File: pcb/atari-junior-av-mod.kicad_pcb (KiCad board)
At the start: 2 copper layers, 50 x 17.5 mm, 36 parts

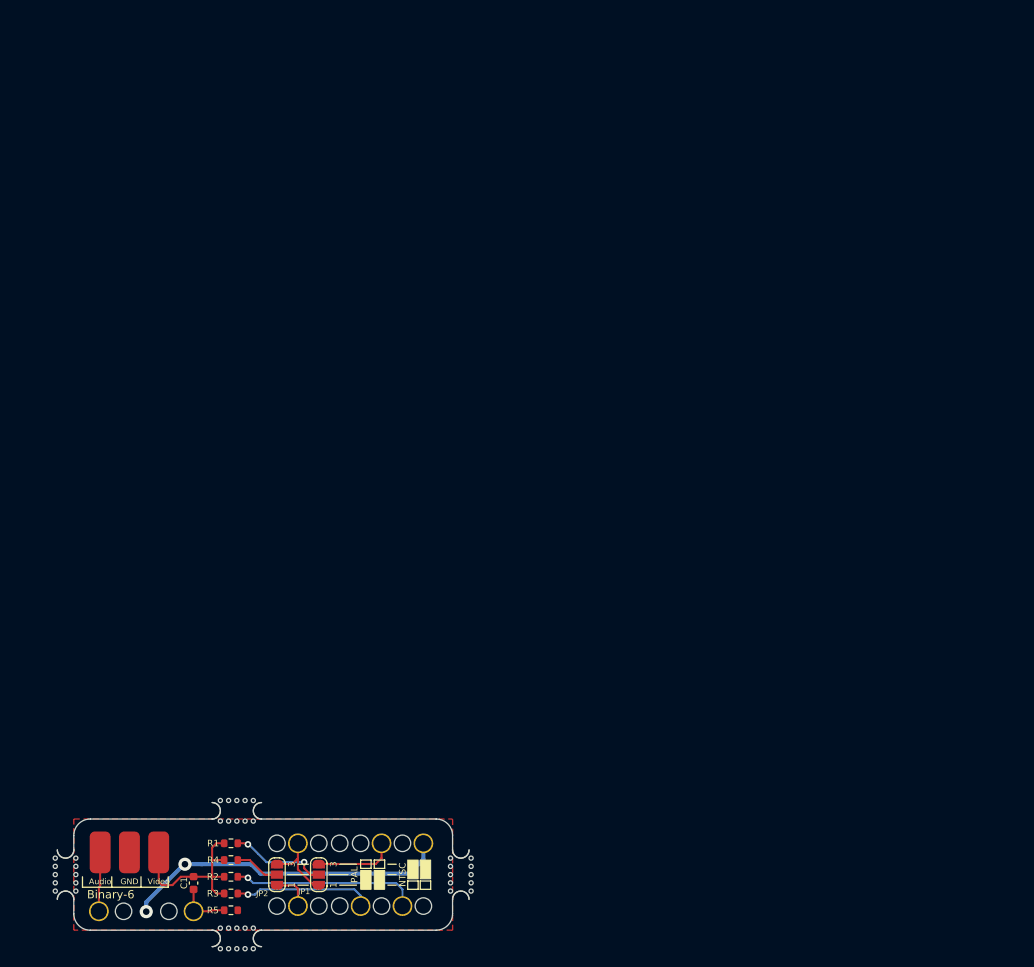
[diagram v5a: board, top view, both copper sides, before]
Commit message: Panelize
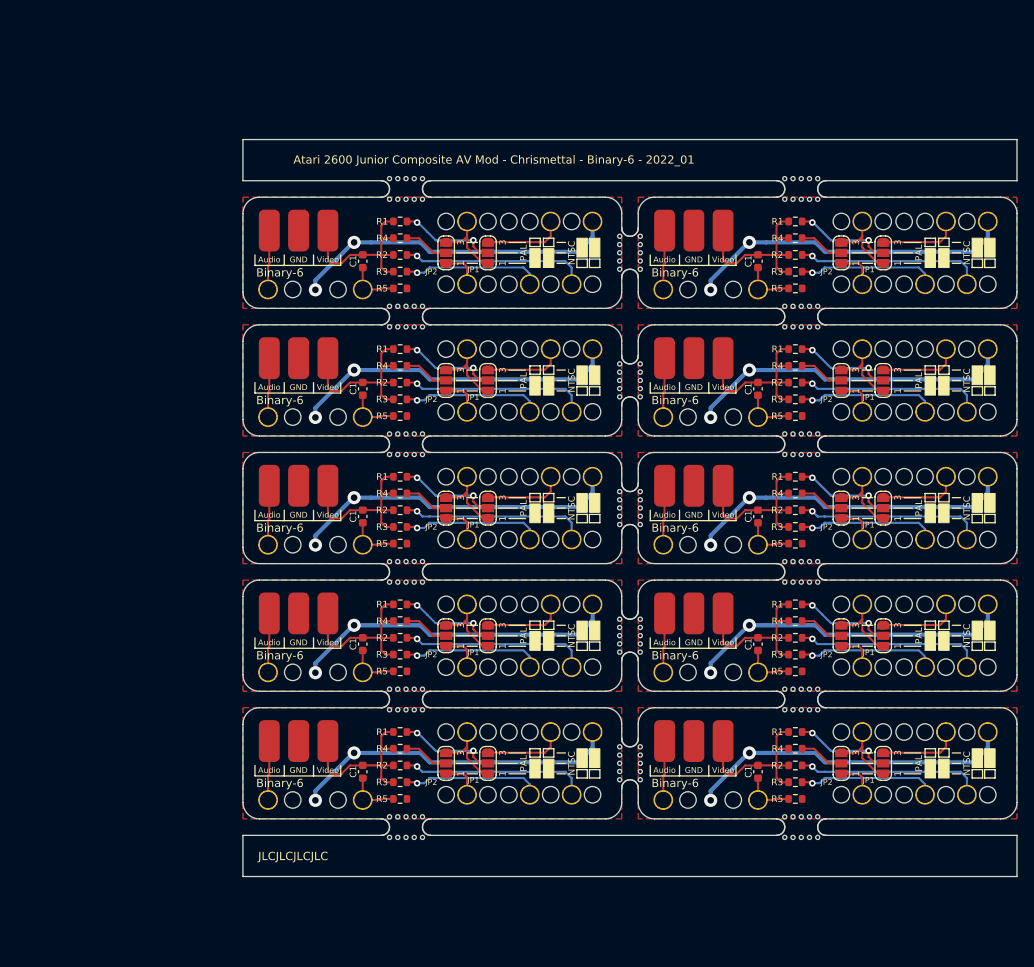
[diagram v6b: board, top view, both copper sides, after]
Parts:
- removed the mouse-bite-1mm-slot at (77.9, 138.0)
- added C1: 100pF, Capacitor_SMD:C_0603_1608Metric, F.Cu at (114.0, 110.0)
- added C1: 100pF, Capacitor_SMD:C_0603_1608Metric, F.Cu at (162.0, 94.5)
- added C1: 100pF, Capacitor_SMD:C_0603_1608Metric, F.Cu at (162.0, 63.5)
- added C1: 100pF, Capacitor_SMD:C_0603_1608Metric, F.Cu at (114.0, 125.5)
- added C1: 100pF, Capacitor_SMD:C_0603_1608Metric, F.Cu at (114.0, 94.5)
- added C1: 100pF, Capacitor_SMD:C_0603_1608Metric, F.Cu at (114.0, 79.0)
- added C1: 100pF, Capacitor_SMD:C_0603_1608Metric, F.Cu at (162.0, 79.0)
- added C1: 100pF, Capacitor_SMD:C_0603_1608Metric, F.Cu at (162.0, 110.0)
- added C1: 100pF, Capacitor_SMD:C_0603_1608Metric, F.Cu at (162.0, 125.5)
- added G***: LOGO, MeineBib:LOGO, B.Cu at (133.0, 78.0)
- added G***: LOGO, MeineBib:LOGO, B.Cu at (133.0, 93.5)
- added G***: LOGO, MeineBib:LOGO, B.Cu at (133.0, 109.0)
- added G***: LOGO, MeineBib:LOGO, B.Cu at (181.0, 109.0)
- added G***: LOGO, MeineBib:LOGO, B.Cu at (133.0, 124.5)
- added G***: LOGO, MeineBib:LOGO, B.Cu at (181.0, 62.5)
- added G***: LOGO, MeineBib:LOGO, B.Cu at (181.0, 93.5)
- added G***: LOGO, MeineBib:LOGO, B.Cu at (181.0, 78.0)
- added G***: LOGO, MeineBib:LOGO, B.Cu at (181.0, 124.5)
- added H1: CD_01, MeineBib:ModHole2mm, F.Cu at (172.2, 58.6)
- added H1: CD_01, MeineBib:ModHole2mm, F.Cu at (124.2, 89.6)
- added H1: CD_01, MeineBib:ModHole2mm, F.Cu at (124.2, 120.6)
- added H1: CD_01, MeineBib:ModHole2mm, F.Cu at (172.2, 120.6)
- added H1: CD_01, MeineBib:ModHole2mm, F.Cu at (172.2, 105.1)
- added H1: CD_01, MeineBib:ModHole2mm, F.Cu at (124.2, 105.1)
- added H1: CD_01, MeineBib:ModHole2mm, F.Cu at (172.2, 74.1)
- added H1: CD_01, MeineBib:ModHole2mm, F.Cu at (172.2, 89.6)
- added H1: CD_01, MeineBib:ModHole2mm, F.Cu at (124.2, 74.1)
- added H10: CD_14, MeineBib:ModHole2mm, F.Cu at (177.2, 97.3)
- added H10: CD_14, MeineBib:ModHole2mm, F.Cu at (177.2, 112.8)
- added H10: CD_14, MeineBib:ModHole2mm, F.Cu at (129.2, 128.3)
- added H10: CD_14, MeineBib:ModHole2mm, F.Cu at (177.2, 81.8)
- added H10: CD_14, MeineBib:ModHole2mm, F.Cu at (129.2, 97.3)
- added H10: CD_14, MeineBib:ModHole2mm, F.Cu at (129.2, 81.8)
- added H10: CD_14, MeineBib:ModHole2mm, F.Cu at (177.2, 66.3)
- added H10: CD_14, MeineBib:ModHole2mm, F.Cu at (129.2, 112.8)
- added H10: CD_14, MeineBib:ModHole2mm, F.Cu at (177.2, 128.3)
- added H11: CD_16, MeineBib:ModHole2mm, F.Cu at (172.2, 81.8)
- added H11: CD_16, MeineBib:ModHole2mm, F.Cu at (124.2, 128.3)
- added H11: CD_16, MeineBib:ModHole2mm, F.Cu at (124.2, 81.8)
- added H11: CD_16, MeineBib:ModHole2mm, F.Cu at (172.2, 97.3)
- added H11: CD_16, MeineBib:ModHole2mm, F.Cu at (172.2, 128.3)
- added H11: CD_16, MeineBib:ModHole2mm, F.Cu at (172.2, 66.3)
- added H11: CD_16, MeineBib:ModHole2mm, F.Cu at (172.2, 112.8)
- added H11: CD_16, MeineBib:ModHole2mm, F.Cu at (124.2, 97.3)
- added H11: CD_16, MeineBib:ModHole2mm, F.Cu at (124.2, 112.8)
- added H12: NC_01, MeineBib:ModHole2mm, F.Cu at (153.5, 82.4)
- added H12: NC_01, MeineBib:ModHole2mm, F.Cu at (105.5, 97.9)
- added H12: NC_01, MeineBib:ModHole2mm, F.Cu at (105.5, 128.9)
- added H12: NC_01, MeineBib:ModHole2mm, F.Cu at (153.5, 66.9)
- added H12: NC_01, MeineBib:ModHole2mm, F.Cu at (153.5, 97.9)
- added H12: NC_01, MeineBib:ModHole2mm, F.Cu at (153.5, 113.4)
- added H12: NC_01, MeineBib:ModHole2mm, F.Cu at (105.5, 82.4)
- added H12: NC_01, MeineBib:ModHole2mm, F.Cu at (153.5, 128.9)
- added H12: NC_01, MeineBib:ModHole2mm, F.Cu at (105.5, 113.4)
- added H13: NC_02, MeineBib:ModHole2mm, F.Cu at (111.0, 97.9)
- added H13: NC_02, MeineBib:ModHole2mm, F.Cu at (159.0, 66.9)
- added H13: NC_02, MeineBib:ModHole2mm, F.Cu at (111.0, 82.4)
- added H13: NC_02, MeineBib:ModHole2mm, F.Cu at (159.0, 82.4)
- added H13: NC_02, MeineBib:ModHole2mm, F.Cu at (111.0, 128.9)
- added H13: NC_02, MeineBib:ModHole2mm, F.Cu at (159.0, 113.4)
- added H13: NC_02, MeineBib:ModHole2mm, F.Cu at (159.0, 97.9)
- added H13: NC_02, MeineBib:ModHole2mm, F.Cu at (159.0, 128.9)
- added H13: NC_02, MeineBib:ModHole2mm, F.Cu at (111.0, 113.4)
- added H2: CD_03, MeineBib:ModHole2mm, F.Cu at (129.2, 120.6)
- added H2: CD_03, MeineBib:ModHole2mm, F.Cu at (177.2, 74.1)
- added H2: CD_03, MeineBib:ModHole2mm, F.Cu at (129.2, 89.6)
- added H2: CD_03, MeineBib:ModHole2mm, F.Cu at (177.2, 89.6)
- added H2: CD_03, MeineBib:ModHole2mm, F.Cu at (177.2, 58.6)
- added H2: CD_03, MeineBib:ModHole2mm, F.Cu at (129.2, 74.1)
- added H2: CD_03, MeineBib:ModHole2mm, F.Cu at (177.2, 120.6)
- added H2: CD_03, MeineBib:ModHole2mm, F.Cu at (177.2, 105.1)
- added H2: CD_03, MeineBib:ModHole2mm, F.Cu at (129.2, 105.1)
- added H3: CD_04, MeineBib:ModHole2mm, F.Cu at (179.8, 74.1)
- added H3: CD_04, MeineBib:ModHole2mm, F.Cu at (179.8, 58.6)
- added H3: CD_04, MeineBib:ModHole2mm, F.Cu at (179.8, 105.1)
- added H3: CD_04, MeineBib:ModHole2mm, F.Cu at (131.8, 74.1)
- added H3: CD_04, MeineBib:ModHole2mm, F.Cu at (179.8, 120.6)
- added H3: CD_04, MeineBib:ModHole2mm, F.Cu at (131.8, 120.6)
- added H3: CD_04, MeineBib:ModHole2mm, F.Cu at (179.8, 89.6)
- added H3: CD_04, MeineBib:ModHole2mm, F.Cu at (131.8, 105.1)
- added H3: CD_04, MeineBib:ModHole2mm, F.Cu at (131.8, 89.6)
- added H4: CD_05, MeineBib:ModHole2mm, F.Cu at (182.3, 89.6)
- added H4: CD_05, MeineBib:ModHole2mm, F.Cu at (182.3, 58.6)
- added H4: CD_05, MeineBib:ModHole2mm, F.Cu at (134.3, 120.6)
- added H4: CD_05, MeineBib:ModHole2mm, F.Cu at (182.3, 105.1)
- added H4: CD_05, MeineBib:ModHole2mm, F.Cu at (134.3, 74.1)
- added H4: CD_05, MeineBib:ModHole2mm, F.Cu at (182.3, 120.6)
- added H4: CD_05, MeineBib:ModHole2mm, F.Cu at (134.3, 89.6)
- added H4: CD_05, MeineBib:ModHole2mm, F.Cu at (134.3, 105.1)
- added H4: CD_05, MeineBib:ModHole2mm, F.Cu at (182.3, 74.1)
- added H6: CD_07, MeineBib:ModHole2mm, F.Cu at (139.4, 89.6)
- added H6: CD_07, MeineBib:ModHole2mm, F.Cu at (187.4, 120.6)
- added H6: CD_07, MeineBib:ModHole2mm, F.Cu at (187.4, 58.6)
- added H6: CD_07, MeineBib:ModHole2mm, F.Cu at (187.4, 74.1)
- added H6: CD_07, MeineBib:ModHole2mm, F.Cu at (139.4, 74.1)
- added H6: CD_07, MeineBib:ModHole2mm, F.Cu at (139.4, 105.1)
- added H6: CD_07, MeineBib:ModHole2mm, F.Cu at (187.4, 89.6)
- added H6: CD_07, MeineBib:ModHole2mm, F.Cu at (139.4, 120.6)
- added H6: CD_07, MeineBib:ModHole2mm, F.Cu at (187.4, 105.1)
- added H7: CD_09, MeineBib:ModHole2mm, F.Cu at (141.9, 112.8)
- added H7: CD_09, MeineBib:ModHole2mm, F.Cu at (141.9, 97.3)
- added H7: CD_09, MeineBib:ModHole2mm, F.Cu at (189.9, 81.8)
- added H7: CD_09, MeineBib:ModHole2mm, F.Cu at (141.9, 128.3)
- added H7: CD_09, MeineBib:ModHole2mm, F.Cu at (189.9, 66.3)
- added H7: CD_09, MeineBib:ModHole2mm, F.Cu at (141.9, 81.8)
- added H7: CD_09, MeineBib:ModHole2mm, F.Cu at (189.9, 112.8)
- added H7: CD_09, MeineBib:ModHole2mm, F.Cu at (189.9, 97.3)
- added H7: CD_09, MeineBib:ModHole2mm, F.Cu at (189.9, 128.3)
- added H8: CD_11, MeineBib:ModHole2mm, F.Cu at (136.8, 128.3)
- added H8: CD_11, MeineBib:ModHole2mm, F.Cu at (184.8, 66.3)
- added H8: CD_11, MeineBib:ModHole2mm, F.Cu at (136.8, 81.8)
- added H8: CD_11, MeineBib:ModHole2mm, F.Cu at (184.8, 81.8)
- added H8: CD_11, MeineBib:ModHole2mm, F.Cu at (184.8, 112.8)
- added H8: CD_11, MeineBib:ModHole2mm, F.Cu at (184.8, 128.3)
- added H8: CD_11, MeineBib:ModHole2mm, F.Cu at (136.8, 112.8)
- added H8: CD_11, MeineBib:ModHole2mm, F.Cu at (136.8, 97.3)
- added H8: CD_11, MeineBib:ModHole2mm, F.Cu at (184.8, 97.3)
- added H9: CD_13, MeineBib:ModHole2mm, F.Cu at (179.8, 97.3)
- added H9: CD_13, MeineBib:ModHole2mm, F.Cu at (179.8, 81.8)
- added H9: CD_13, MeineBib:ModHole2mm, F.Cu at (179.8, 66.3)
- added H9: CD_13, MeineBib:ModHole2mm, F.Cu at (131.8, 81.8)
- added H9: CD_13, MeineBib:ModHole2mm, F.Cu at (131.8, 112.8)
- added H9: CD_13, MeineBib:ModHole2mm, F.Cu at (179.8, 128.3)
- added H9: CD_13, MeineBib:ModHole2mm, F.Cu at (179.8, 112.8)
- added H9: CD_13, MeineBib:ModHole2mm, F.Cu at (131.8, 128.3)
- added H9: CD_13, MeineBib:ModHole2mm, F.Cu at (131.8, 97.3)
- added JP1: JP_3_Open, Jumper:SolderJumper-3_P1.3mm_Open_RoundedPad1.0x1.5mm_NumberLabels, F.Cu at (129.2, 93.5)
- added JP1: JP_3_Open, Jumper:SolderJumper-3_P1.3mm_Open_RoundedPad1.0x1.5mm_NumberLabels, F.Cu at (129.2, 109.0)
- added JP1: JP_3_Open, Jumper:SolderJumper-3_P1.3mm_Open_RoundedPad1.0x1.5mm_NumberLabels, F.Cu at (129.2, 124.5)
- added JP1: JP_3_Open, Jumper:SolderJumper-3_P1.3mm_Open_RoundedPad1.0x1.5mm_NumberLabels, F.Cu at (177.2, 93.5)
- added JP1: JP_3_Open, Jumper:SolderJumper-3_P1.3mm_Open_RoundedPad1.0x1.5mm_NumberLabels, F.Cu at (177.2, 109.0)
- added JP1: JP_3_Open, Jumper:SolderJumper-3_P1.3mm_Open_RoundedPad1.0x1.5mm_NumberLabels, F.Cu at (177.2, 78.0)
- added JP1: JP_3_Open, Jumper:SolderJumper-3_P1.3mm_Open_RoundedPad1.0x1.5mm_NumberLabels, F.Cu at (177.2, 62.5)
- added JP1: JP_3_Open, Jumper:SolderJumper-3_P1.3mm_Open_RoundedPad1.0x1.5mm_NumberLabels, F.Cu at (129.2, 78.0)
- added JP1: JP_3_Open, Jumper:SolderJumper-3_P1.3mm_Open_RoundedPad1.0x1.5mm_NumberLabels, F.Cu at (177.2, 124.5)
- added JP2: JP_3_Open, Jumper:SolderJumper-3_P1.3mm_Open_RoundedPad1.0x1.5mm_NumberLabels, F.Cu at (124.2, 124.5)
- added JP2: JP_3_Open, Jumper:SolderJumper-3_P1.3mm_Open_RoundedPad1.0x1.5mm_NumberLabels, F.Cu at (124.2, 78.0)
- added JP2: JP_3_Open, Jumper:SolderJumper-3_P1.3mm_Open_RoundedPad1.0x1.5mm_NumberLabels, F.Cu at (172.2, 109.0)
- added JP2: JP_3_Open, Jumper:SolderJumper-3_P1.3mm_Open_RoundedPad1.0x1.5mm_NumberLabels, F.Cu at (172.2, 78.0)
- added JP2: JP_3_Open, Jumper:SolderJumper-3_P1.3mm_Open_RoundedPad1.0x1.5mm_NumberLabels, F.Cu at (172.2, 62.5)
- added JP2: JP_3_Open, Jumper:SolderJumper-3_P1.3mm_Open_RoundedPad1.0x1.5mm_NumberLabels, F.Cu at (124.2, 93.5)
- added JP2: JP_3_Open, Jumper:SolderJumper-3_P1.3mm_Open_RoundedPad1.0x1.5mm_NumberLabels, F.Cu at (172.2, 93.5)
- added JP2: JP_3_Open, Jumper:SolderJumper-3_P1.3mm_Open_RoundedPad1.0x1.5mm_NumberLabels, F.Cu at (124.2, 109.0)
- added JP2: JP_3_Open, Jumper:SolderJumper-3_P1.3mm_Open_RoundedPad1.0x1.5mm_NumberLabels, F.Cu at (172.2, 124.5)
- added Pad1: Audio, MeineBib:ModWirePad, F.Cu at (150.7, 106.2)
- added Pad1: Audio, MeineBib:ModWirePad, F.Cu at (102.7, 121.7)
- added Pad1: Audio, MeineBib:ModWirePad, F.Cu at (150.7, 75.2)
- added Pad1: Audio, MeineBib:ModWirePad, F.Cu at (102.7, 75.2)
- added Pad1: Audio, MeineBib:ModWirePad, F.Cu at (150.7, 121.7)
- added Pad1: Audio, MeineBib:ModWirePad, F.Cu at (150.7, 59.7)
- added Pad1: Audio, MeineBib:ModWirePad, F.Cu at (102.7, 106.2)
- added Pad1: Audio, MeineBib:ModWirePad, F.Cu at (102.7, 90.7)
- added Pad1: Audio, MeineBib:ModWirePad, F.Cu at (150.7, 90.7)
- added Pad10: Color, MeineBib:ModPad2mm, F.Cu at (162.0, 66.9)
- added Pad10: Color, MeineBib:ModPad2mm, F.Cu at (162.0, 128.9)
- added Pad10: Color, MeineBib:ModPad2mm, F.Cu at (162.0, 113.4)
- added Pad10: Color, MeineBib:ModPad2mm, F.Cu at (162.0, 97.9)
- added Pad10: Color, MeineBib:ModPad2mm, F.Cu at (114.0, 82.4)
- added Pad10: Color, MeineBib:ModPad2mm, F.Cu at (162.0, 82.4)
- added Pad10: Color, MeineBib:ModPad2mm, F.Cu at (114.0, 97.9)
- added Pad10: Color, MeineBib:ModPad2mm, F.Cu at (114.0, 113.4)
- added Pad10: Color, MeineBib:ModPad2mm, F.Cu at (114.0, 128.9)
- added Pad11: CD_08, MeineBib:ModPad2mm, F.Cu at (141.9, 74.1)
- added Pad11: CD_08, MeineBib:ModPad2mm, F.Cu at (189.9, 89.6)
- added Pad11: CD_08, MeineBib:ModPad2mm, F.Cu at (141.9, 89.6)
- added Pad11: CD_08, MeineBib:ModPad2mm, F.Cu at (189.9, 105.1)
- added Pad11: CD_08, MeineBib:ModPad2mm, F.Cu at (189.9, 58.6)
- added Pad11: CD_08, MeineBib:ModPad2mm, F.Cu at (189.9, 74.1)
- added Pad11: CD_08, MeineBib:ModPad2mm, F.Cu at (189.9, 120.6)
- added Pad11: CD_08, MeineBib:ModPad2mm, F.Cu at (141.9, 105.1)
- added Pad11: CD_08, MeineBib:ModPad2mm, F.Cu at (141.9, 120.6)
- added Pad2: GND, MeineBib:ModWirePad, F.Cu at (154.2, 75.2)
- added Pad2: GND, MeineBib:ModWirePad, F.Cu at (154.2, 90.7)
- added Pad2: GND, MeineBib:ModWirePad, F.Cu at (106.2, 75.2)
- added Pad2: GND, MeineBib:ModWirePad, F.Cu at (154.2, 59.7)
- added Pad2: GND, MeineBib:ModWirePad, F.Cu at (154.2, 121.7)
- added Pad2: GND, MeineBib:ModWirePad, F.Cu at (106.2, 106.2)
- added Pad2: GND, MeineBib:ModWirePad, F.Cu at (106.2, 121.7)
- added Pad2: GND, MeineBib:ModWirePad, F.Cu at (106.2, 90.7)
- added Pad2: GND, MeineBib:ModWirePad, F.Cu at (154.2, 106.2)
- added Pad3: Video, MeineBib:ModWirePad, F.Cu at (157.8, 75.2)
- added Pad3: Video, MeineBib:ModWirePad, F.Cu at (157.8, 106.2)
- added Pad3: Video, MeineBib:ModWirePad, F.Cu at (109.8, 75.2)
- added Pad3: Video, MeineBib:ModWirePad, F.Cu at (157.8, 90.7)
- added Pad3: Video, MeineBib:ModWirePad, F.Cu at (109.8, 121.7)
- added Pad3: Video, MeineBib:ModWirePad, F.Cu at (109.8, 90.7)
- added Pad3: Video, MeineBib:ModWirePad, F.Cu at (157.8, 121.7)
- added Pad3: Video, MeineBib:ModWirePad, F.Cu at (109.8, 106.2)
- added Pad3: Video, MeineBib:ModWirePad, F.Cu at (157.8, 59.7)
- added Pad4: Audio, MeineBib:ModPad2mm, F.Cu at (150.5, 113.4)
- added Pad4: Audio, MeineBib:ModPad2mm, F.Cu at (150.5, 82.4)
- added Pad4: Audio, MeineBib:ModPad2mm, F.Cu at (102.5, 128.9)
- added Pad4: Audio, MeineBib:ModPad2mm, F.Cu at (102.5, 113.4)
- added Pad4: Audio, MeineBib:ModPad2mm, F.Cu at (102.5, 82.4)
- added Pad4: Audio, MeineBib:ModPad2mm, F.Cu at (102.5, 97.9)
- added Pad4: Audio, MeineBib:ModPad2mm, F.Cu at (150.5, 66.9)
- added Pad4: Audio, MeineBib:ModPad2mm, F.Cu at (150.5, 97.9)
- added Pad4: Audio, MeineBib:ModPad2mm, F.Cu at (150.5, 128.9)
- added Pad5: CD_10, MeineBib:ModPad2mm, F.Cu at (187.4, 112.8)
- added Pad5: CD_10, MeineBib:ModPad2mm, F.Cu at (139.4, 128.3)
- added Pad5: CD_10, MeineBib:ModPad2mm, F.Cu at (187.4, 97.3)
- added Pad5: CD_10, MeineBib:ModPad2mm, F.Cu at (187.4, 128.3)
- added Pad5: CD_10, MeineBib:ModPad2mm, F.Cu at (139.4, 81.8)
- added Pad5: CD_10, MeineBib:ModPad2mm, F.Cu at (187.4, 66.3)
- added Pad5: CD_10, MeineBib:ModPad2mm, F.Cu at (139.4, 97.3)
- added Pad5: CD_10, MeineBib:ModPad2mm, F.Cu at (139.4, 112.8)
- added Pad5: CD_10, MeineBib:ModPad2mm, F.Cu at (187.4, 81.8)
- added Pad6: CD_12, MeineBib:ModPad2mm, F.Cu at (134.3, 128.3)
- added Pad6: CD_12, MeineBib:ModPad2mm, F.Cu at (182.3, 97.3)
- added Pad6: CD_12, MeineBib:ModPad2mm, F.Cu at (182.3, 112.8)
- added Pad6: CD_12, MeineBib:ModPad2mm, F.Cu at (182.3, 66.3)
- added Pad6: CD_12, MeineBib:ModPad2mm, F.Cu at (134.3, 97.3)
- added Pad6: CD_12, MeineBib:ModPad2mm, F.Cu at (182.3, 81.8)
- added Pad6: CD_12, MeineBib:ModPad2mm, F.Cu at (182.3, 128.3)
- added Pad6: CD_12, MeineBib:ModPad2mm, F.Cu at (134.3, 112.8)
- added Pad6: CD_12, MeineBib:ModPad2mm, F.Cu at (134.3, 81.8)
- added Pad7: CD_06, MeineBib:ModPad2mm, F.Cu at (136.8, 74.1)
- added Pad7: CD_06, MeineBib:ModPad2mm, F.Cu at (136.8, 89.6)
- added Pad7: CD_06, MeineBib:ModPad2mm, F.Cu at (184.8, 120.6)
- added Pad7: CD_06, MeineBib:ModPad2mm, F.Cu at (184.8, 105.1)
- added Pad7: CD_06, MeineBib:ModPad2mm, F.Cu at (184.8, 74.1)
- added Pad7: CD_06, MeineBib:ModPad2mm, F.Cu at (184.8, 89.6)
- added Pad7: CD_06, MeineBib:ModPad2mm, F.Cu at (136.8, 105.1)
- added Pad7: CD_06, MeineBib:ModPad2mm, F.Cu at (184.8, 58.6)
- added Pad7: CD_06, MeineBib:ModPad2mm, F.Cu at (136.8, 120.6)
- added Pad8: CD_02, MeineBib:ModPad2mm, F.Cu at (126.7, 105.1)
- added Pad8: CD_02, MeineBib:ModPad2mm, F.Cu at (126.7, 89.6)
- added Pad8: CD_02, MeineBib:ModPad2mm, F.Cu at (174.7, 105.1)
- added Pad8: CD_02, MeineBib:ModPad2mm, F.Cu at (174.7, 120.6)
- added Pad8: CD_02, MeineBib:ModPad2mm, F.Cu at (174.7, 58.6)
- added Pad8: CD_02, MeineBib:ModPad2mm, F.Cu at (174.7, 89.6)
- added Pad8: CD_02, MeineBib:ModPad2mm, F.Cu at (126.7, 120.6)
- added Pad8: CD_02, MeineBib:ModPad2mm, F.Cu at (174.7, 74.1)
- added Pad8: CD_02, MeineBib:ModPad2mm, F.Cu at (126.7, 74.1)
- added Pad9: CD_15, MeineBib:ModPad2mm, F.Cu at (126.7, 97.3)
- added Pad9: CD_15, MeineBib:ModPad2mm, F.Cu at (174.7, 97.3)
- added Pad9: CD_15, MeineBib:ModPad2mm, F.Cu at (126.7, 112.8)
- added Pad9: CD_15, MeineBib:ModPad2mm, F.Cu at (174.7, 128.3)
- added Pad9: CD_15, MeineBib:ModPad2mm, F.Cu at (126.7, 81.8)
- added Pad9: CD_15, MeineBib:ModPad2mm, F.Cu at (126.7, 128.3)
- added Pad9: CD_15, MeineBib:ModPad2mm, F.Cu at (174.7, 81.8)
- added Pad9: CD_15, MeineBib:ModPad2mm, F.Cu at (174.7, 66.3)
- added Pad9: CD_15, MeineBib:ModPad2mm, F.Cu at (174.7, 112.8)
- added R1: 3.3K, Resistor_SMD:R_0603_1608Metric, F.Cu at (166.6, 120.6)
- added R1: 3.3K, Resistor_SMD:R_0603_1608Metric, F.Cu at (166.6, 74.1)
- added R1: 3.3K, Resistor_SMD:R_0603_1608Metric, F.Cu at (118.6, 105.1)
- added R1: 3.3K, Resistor_SMD:R_0603_1608Metric, F.Cu at (166.6, 58.6)
- added R1: 3.3K, Resistor_SMD:R_0603_1608Metric, F.Cu at (118.6, 120.6)
- added R1: 3.3K, Resistor_SMD:R_0603_1608Metric, F.Cu at (118.6, 89.6)
- added R1: 3.3K, Resistor_SMD:R_0603_1608Metric, F.Cu at (166.6, 89.6)
- added R1: 3.3K, Resistor_SMD:R_0603_1608Metric, F.Cu at (118.6, 74.1)
- added R1: 3.3K, Resistor_SMD:R_0603_1608Metric, F.Cu at (166.6, 105.1)
- added R2: 2.2K, Resistor_SMD:R_0603_1608Metric, F.Cu at (118.6, 124.7)
- added R2: 2.2K, Resistor_SMD:R_0603_1608Metric, F.Cu at (166.6, 124.7)
- added R2: 2.2K, Resistor_SMD:R_0603_1608Metric, F.Cu at (166.6, 109.2)
- added R2: 2.2K, Resistor_SMD:R_0603_1608Metric, F.Cu at (166.6, 93.7)
- added R2: 2.2K, Resistor_SMD:R_0603_1608Metric, F.Cu at (166.6, 78.2)
- added R2: 2.2K, Resistor_SMD:R_0603_1608Metric, F.Cu at (118.6, 93.7)
- added R2: 2.2K, Resistor_SMD:R_0603_1608Metric, F.Cu at (166.6, 62.7)
- added R2: 2.2K, Resistor_SMD:R_0603_1608Metric, F.Cu at (118.6, 109.2)
- added R2: 2.2K, Resistor_SMD:R_0603_1608Metric, F.Cu at (118.6, 78.2)
- added R3: 330R, Resistor_SMD:R_0603_1608Metric, F.Cu at (118.6, 80.2)
- added R3: 330R, Resistor_SMD:R_0603_1608Metric, F.Cu at (118.6, 111.2)
- added R3: 330R, Resistor_SMD:R_0603_1608Metric, F.Cu at (166.6, 80.2)
- added R3: 330R, Resistor_SMD:R_0603_1608Metric, F.Cu at (166.6, 64.7)
- added R3: 330R, Resistor_SMD:R_0603_1608Metric, F.Cu at (166.6, 95.7)
- added R3: 330R, Resistor_SMD:R_0603_1608Metric, F.Cu at (166.6, 126.7)
- added R3: 330R, Resistor_SMD:R_0603_1608Metric, F.Cu at (118.6, 95.7)
- added R3: 330R, Resistor_SMD:R_0603_1608Metric, F.Cu at (118.6, 126.7)
- added R3: 330R, Resistor_SMD:R_0603_1608Metric, F.Cu at (166.6, 111.2)
- added R4: 1K, Resistor_SMD:R_0603_1608Metric, F.Cu at (166.6, 76.2)
- added R4: 1K, Resistor_SMD:R_0603_1608Metric, F.Cu at (118.6, 91.7)
- added R4: 1K, Resistor_SMD:R_0603_1608Metric, F.Cu at (118.6, 107.2)
- added R4: 1K, Resistor_SMD:R_0603_1608Metric, F.Cu at (166.6, 60.7)
- added R4: 1K, Resistor_SMD:R_0603_1608Metric, F.Cu at (166.6, 122.7)
- added R4: 1K, Resistor_SMD:R_0603_1608Metric, F.Cu at (118.6, 122.7)
- added R4: 1K, Resistor_SMD:R_0603_1608Metric, F.Cu at (118.6, 76.2)
- added R4: 1K, Resistor_SMD:R_0603_1608Metric, F.Cu at (166.6, 107.2)
- added R4: 1K, Resistor_SMD:R_0603_1608Metric, F.Cu at (166.6, 91.7)
- added R5: 1K, Resistor_SMD:R_0603_1608Metric, F.Cu at (166.6, 66.8)
- added R5: 1K, Resistor_SMD:R_0603_1608Metric, F.Cu at (118.6, 128.8)
- added R5: 1K, Resistor_SMD:R_0603_1608Metric, F.Cu at (118.6, 97.8)
- added R5: 1K, Resistor_SMD:R_0603_1608Metric, F.Cu at (166.6, 113.3)
- added R5: 1K, Resistor_SMD:R_0603_1608Metric, F.Cu at (166.6, 97.8)
- added R5: 1K, Resistor_SMD:R_0603_1608Metric, F.Cu at (118.6, 113.3)
- added R5: 1K, Resistor_SMD:R_0603_1608Metric, F.Cu at (166.6, 128.8)
- added R5: 1K, Resistor_SMD:R_0603_1608Metric, F.Cu at (118.6, 82.3)
- added R5: 1K, Resistor_SMD:R_0603_1608Metric, F.Cu at (166.6, 82.3)
- added mouse-bite-1mm-slot: VAL**, MeineBib:mouse-bite-2mm-slot_4mm_space, F.Cu at (119.3, 116.7)
- added mouse-bite-1mm-slot: VAL**, MeineBib:mouse-bite-2mm-slot_4mm_space, F.Cu at (146.5, 124.4)
- added mouse-bite-1mm-slot: VAL**, MeineBib:mouse-bite-2mm-slot_4mm_space, F.Cu at (167.3, 70.2)
- added mouse-bite-1mm-slot: VAL**, MeineBib:mouse-bite-2mm-slot_4mm_space, F.Cu at (119.3, 101.2)
- added mouse-bite-1mm-slot: VAL**, MeineBib:mouse-bite-2mm-slot_4mm_space, F.Cu at (146.5, 108.9)
- added mouse-bite-1mm-slot: VAL**, MeineBib:mouse-bite-2mm-slot_4mm_space, F.Cu at (146.5, 77.9)
- added mouse-bite-1mm-slot: VAL**, MeineBib:mouse-bite-2mm-slot_4mm_space, F.Cu at (167.3, 116.7)
- added mouse-bite-1mm-slot: VAL**, MeineBib:mouse-bite-2mm-slot_4mm_space, F.Cu at (119.3, 85.7)
- added mouse-bite-1mm-slot: VAL**, MeineBib:mouse-bite-2mm-slot_4mm_space, F.Cu at (119.3, 132.2)
- added mouse-bite-1mm-slot: VAL**, MeineBib:mouse-bite-2mm-slot_4mm_space, F.Cu at (146.5, 93.4)
- added mouse-bite-1mm-slot: VAL**, MeineBib:mouse-bite-2mm-slot_4mm_space, F.Cu at (167.3, 85.7)
- added mouse-bite-1mm-slot: VAL**, MeineBib:mouse-bite-2mm-slot_4mm_space, F.Cu at (167.3, 101.2)
- added mouse-bite-1mm-slot: VAL**, MeineBib:mouse-bite-2mm-slot_4mm_space, F.Cu at (167.3, 132.2)
- added mouse-bite-1mm-slot4: VAL**, MeineBib:mouse-bite-2mm-slot_4mm_space, F.Cu at (167.3, 54.7)
- moved G*** 78.3 mm to (133.0, 62.5)
- moved H10 78.3 mm to (129.2, 66.3)
- moved H11 78.3 mm to (124.2, 66.3)
- moved H7 78.3 mm to (141.9, 66.3)
- moved H8 78.3 mm to (136.8, 66.3)
- moved H9 78.3 mm to (131.8, 66.3)
- moved JP1 78.3 mm to (129.2, 62.5)
- moved JP2 78.3 mm to (124.2, 62.5)
- moved Pad5 78.3 mm to (139.4, 66.3)
- moved Pad6 78.3 mm to (134.3, 66.3)
- moved Pad9 78.3 mm to (126.7, 66.3)
- moved R4 78.3 mm to (118.6, 60.7)
- moved mouse-bite-1mm-slot 78.3 mm to (146.5, 62.4)
- moved mouse-bite-1mm-slot 78.3 mm to (119.3, 54.7)
- moved mouse-bite-1mm-slot 78.3 mm to (119.3, 70.2)
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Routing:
- net GND: track 39.9 -> 398.5 mm, vias 2 -> 20
- net /Lum1: track 22.7 -> 226.7 mm, vias 1 -> 10
- net Net-(C1-Pad1): track 22.0 -> 220.0 mm
- net /Sync: track 16.8 -> 168.2 mm, vias 1 -> 10
- net /Lum0: track 11.9 -> 118.6 mm, vias 2 -> 20
- net Net-(JP1-Pad3): track 9.72 -> 97.2 mm
- net Net-(JP1-Pad1): track 9.34 -> 93.4 mm
- net /Audio: track 7.22 -> 72.2 mm
- net /Color: track 6.42 -> 64.2 mm
- net /Lum2: track 5.50 -> 55.0 mm
- net Net-(JP2-Pad1): track 4.82 -> 48.2 mm
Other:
- board size 50 x 17.5 mm -> 94 x 89.5 mm
- board text added: "Atari 2600 Junior Composite AV Mod - Chrismettal - Binary-6 - 2022_01"
- board text added: "JLCJLCJLCJLC"

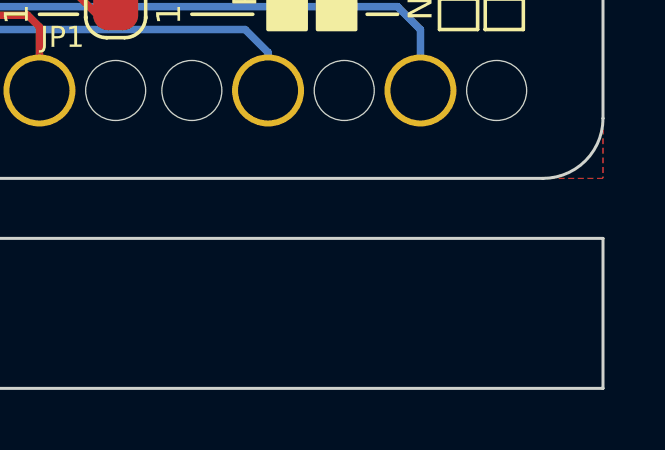
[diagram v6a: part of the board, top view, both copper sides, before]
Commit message: Add git version hash
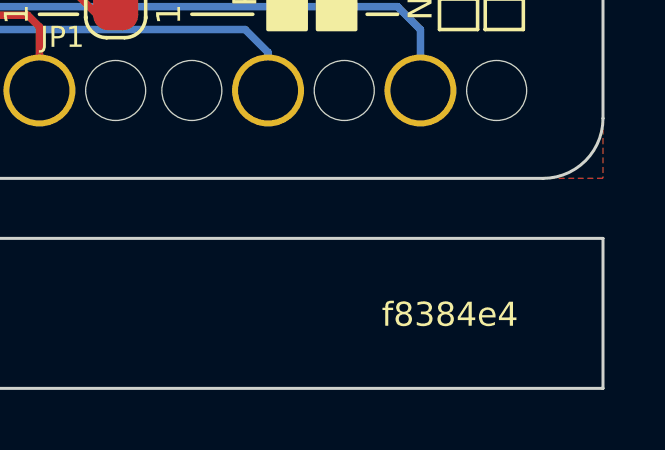
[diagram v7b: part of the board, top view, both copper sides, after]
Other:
- board text added: "f8384e4"
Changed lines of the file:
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@@
+    (effects (font (size 0.8 0.8) (thickness 0.12)))
+  )
+  (gr_text "f8384e4" (at 188.375 135.7355) (layer "F.SilkS")
     (effects (font (size 0.8 0.8) (thickness 0.12)))
   )
